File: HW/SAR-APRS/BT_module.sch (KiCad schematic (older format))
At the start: 6 parts

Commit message: schematic update
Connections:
- no-connect marks 0 -> 1
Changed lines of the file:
@@
 Text GLabel 4650 2975 0    50   Input ~ 0
 BT_LED2
+NoConn ~ 5575 3825
 $EndSCHEMATC

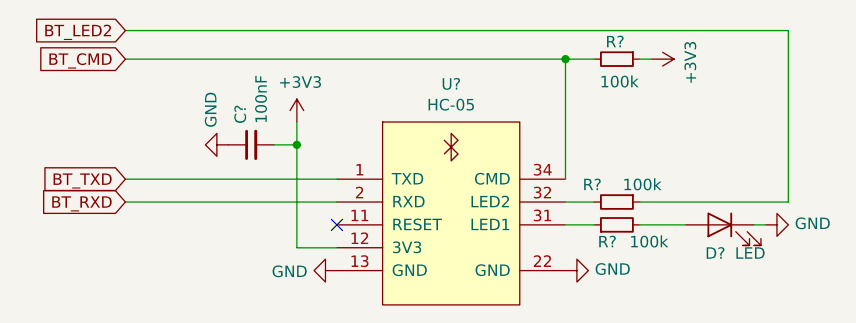
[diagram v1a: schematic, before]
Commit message: schematic update
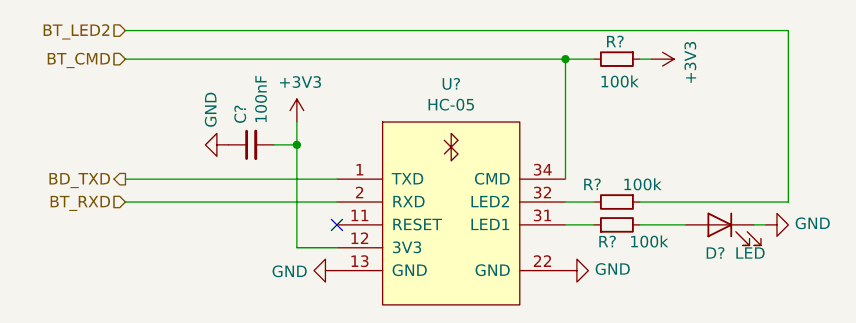
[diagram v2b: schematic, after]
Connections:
- net BT_TXD renamed BD_TXD
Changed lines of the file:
@@
 $Descr A4 11693 8268
 encoding utf-8
-Sheet 6 6
+Sheet 5 6
 Title ""
 Date ""
@@
 Wire Wire Line
 	4650 2975 7550 2975
-Text GLabel 4650 3100 0    50   Input ~ 0
-BT_CMD
 Wire Wire Line
 	4650 3100 6575 3100
-Text GLabel 4650 3625 0    50   Input ~ 0
-BT_TXD
-Text GLabel 4650 3725 0    50   Input ~ 0
-BT_RXD
 Wire Wire Line
 	4650 3625 5575 3625
 Wire Wire Line
 	4650 3725 5575 3725
-Text GLabel 4650 2975 0    50   Input ~ 0
+NoConn ~ 5575 3825
+Text HLabel 4650 2975 0    50   Input ~ 0
 BT_LED2
-NoConn ~ 5575 3825
+Text HLabel 4650 3100 0    50   Input ~ 0
+BT_CMD
+Text HLabel 4650 3625 0    50   Output ~ 0
+BD_TXD
+Text HLabel 4650 3725 0    50   Input ~ 0
+BT_RXD
 $EndSCHEMATC

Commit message: schem and pcb update
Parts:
- gave numbers to parts that had none: 6
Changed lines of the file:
@@
 EESchema Schematic File Version 4
 LIBS:SAR-APRS-cache
-EELAYER 28 0
+EELAYER 29 0
 EELAYER END
 $Descr A4 11693 8268
@@
 $EndDescr
 $Comp
-L power:GND #PWR?
+L power:GND #PWR0142
 U 1 1 5C823DC3
 P 5575 4025
-F 0 "#PWR?" H 5575 3775 50  0001 C CNN
+F 0 "#PWR0142" H 5575 3775 50  0001 C CNN
 F 1 "GND" V 5580 3897 50  0000 R CNN
 F 2 "" H 5575 4025 50  0001 C CNN
@@
 $EndComp
 $Comp
-L power:+3V3 #PWR?
+L power:+3V3 #PWR0143
 U 1 1 5C823DC9
 P 5400 3375
-F 0 "#PWR?" H 5400 3225 50  0001 C CNN
+F 0 "#PWR0143" H 5400 3225 50  0001 C CNN
 F 1 "+3V3" H 5415 3548 50  0000 C CNN
 F 2 "" H 5400 3375 50  0001 C CNN
@@
 	5400 3925 5400 3475
 $Comp
-L device:C_Small C?
+L device:C_Small C22
 U 1 1 5C823DD1
 P 5200 3475
-F 0 "C?" H 5292 3521 50  0000 L CNN
+F 0 "C22" H 5292 3521 50  0000 L CNN
 F 1 "100nF" H 5292 3430 50  0000 L CNN
 F 2 "" H 5200 3475 50  0001 C CNN
@@
 $EndComp
 $Comp
-L power:GND #PWR?
+L power:GND #PWR0144
 U 1 1 5C823DD7
 P 5100 3475
-F 0 "#PWR?" H 5100 3225 50  0001 C CNN
+F 0 "#PWR0144" H 5100 3225 50  0001 C CNN
 F 1 "GND" H 5025 3400 50  0000 R CNN
 F 2 "" H 5100 3475 50  0001 C CNN
@@
 	5300 3475 5400 3475
 $Comp
-L power:GND #PWR?
+L power:GND #PWR0145
 U 1 1 5C823DE0
 P 6575 4025
-F 0 "#PWR?" H 6575 3775 50  0001 C CNN
+F 0 "#PWR0145" H 6575 3775 50  0001 C CNN
 F 1 "GND" V 6580 3897 50  0000 R CNN
 F 2 "" H 6575 4025 50  0001 C CNN
@@
 $EndComp
 $Comp
-L device:R_Small R?
+L device:R_Small R24
 U 1 1 5C823DE6
 P 6800 3725
-F 0 "R?" V 6725 3575 50  0000 L CNN
+F 0 "R24" V 6725 3575 50  0000 L CNN
 F 1 "100k" V 6725 3750 50  0000 L CNN
 F 2 "" H 6800 3725 50  0001 C CNN
@@
 $EndComp
 $Comp
-L device:R_Small R?
+L device:R_Small R25
 U 1 1 5C823DEC
 P 6800 3825
-F 0 "R?" V 6725 3825 50  0000 L CNN
+F 0 "R25" V 6725 3825 50  0000 L CNN
 F 1 "100k" V 6725 3600 50  0000 L CNN
 F 2 "" H 6800 3825 50  0001 C CNN
@@
 	6700 3825 6575 3825
 $Comp
-L device:LED D?
+L device:LED D6
 U 1 1 5C823DF4
 P 7250 3825
-F 0 "D?" H 7225 3700 50  0000 L CNN
+F 0 "D6" H 7225 3700 50  0000 L CNN
 F 1 "LED" H 7050 3700 50  0000 L CNN
 F 2 "" H 7250 3825 50  0001 C CNN
@@
 	7450 3825 7400 3825
 $Comp
-L power:GND #PWR?
+L power:GND #PWR0146
 U 1 1 5C823DFC
 P 7450 3825
-F 0 "#PWR?" H 7450 3575 50  0001 C CNN
+F 0 "#PWR0146" H 7450 3575 50  0001 C CNN
 F 1 "GND" V 7455 3697 50  0000 R CNN
 F 2 "" H 7450 3825 50  0001 C CNN
@@
 $EndComp
 $Comp
-L power:+3V3 #PWR?
+L power:+3V3 #PWR0147
 U 1 1 5C823E02
 P 6950 3100
-F 0 "#PWR?" H 6950 2950 50  0001 C CNN
+F 0 "#PWR0147" H 6950 2950 50  0001 C CNN
 F 1 "+3V3" H 6965 3273 50  0000 C CNN
 F 2 "" H 6950 3100 50  0001 C CNN
@@
 $EndComp
 $Comp
-L APRS_modules:HC-05 U?
+L APRS_modules:HC-05 U8
 U 1 1 5C823E09
 P 6075 3825
-F 0 "U?" H 6075 4440 50  0000 C CNN
+F 0 "U8" H 6075 4440 50  0000 C CNN
 F 1 "HC-05" H 6075 4349 50  0000 C CNN
 F 2 "maxrez:HC-05 BT" H 5575 4175 50  0001 C CNN
@@
 	6950 3100 6900 3100
 $Comp
-L device:R_Small R?
+L device:R_Small R23
 U 1 1 5C823E15
 P 6800 3100
-F 0 "R?" V 6725 3050 50  0000 L CNN
+F 0 "R23" V 6725 3050 50  0000 L CNN
 F 1 "100k" V 6900 3025 50  0000 L CNN
 F 2 "" H 6800 3100 50  0001 C CNN

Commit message: schm and pcb update
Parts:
- C22: footprint (none) -> Capacitors_SMD:C_0603
- R23, R24, R25: footprint (none) -> Resistors_SMD:R_0603
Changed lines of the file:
@@
 F 0 "C22" H 5292 3521 50  0000 L CNN
 F 1 "100nF" H 5292 3430 50  0000 L CNN
-F 2 "" H 5200 3475 50  0001 C CNN
+F 2 "Capacitors_SMD:C_0603" H 5200 3475 50  0001 C CNN
 F 3 "~" H 5200 3475 50  0001 C CNN
 	1    5200 3475
@@
 F 0 "R24" V 6725 3575 50  0000 L CNN
 F 1 "100k" V 6725 3750 50  0000 L CNN
-F 2 "" H 6800 3725 50  0001 C CNN
+F 2 "Resistors_SMD:R_0603" H 6800 3725 50  0001 C CNN
 F 3 "~" H 6800 3725 50  0001 C CNN
 	1    6800 3725
@@
 F 0 "R25" V 6725 3825 50  0000 L CNN
 F 1 "100k" V 6725 3600 50  0000 L CNN
-F 2 "" H 6800 3825 50  0001 C CNN
+F 2 "Resistors_SMD:R_0603" H 6800 3825 50  0001 C CNN
 F 3 "~" H 6800 3825 50  0001 C CNN
 	1    6800 3825
@@
 F 0 "R23" V 6725 3050 50  0000 L CNN
 F 1 "100k" V 6900 3025 50  0000 L CNN
-F 2 "" H 6800 3100 50  0001 C CNN
+F 2 "Resistors_SMD:R_0603" H 6800 3100 50  0001 C CNN
 F 3 "~" H 6800 3100 50  0001 C CNN
 	1    6800 3100

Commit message: PCB update
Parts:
- C22: footprint Capacitors_SMD:C_0603 -> Capacitors_SMD:C_0805
- D6: footprint (none) -> LEDs:LED_0805
- R23, R24, R25: footprint Resistors_SMD:R_0603 -> Resistors_SMD:R_0805
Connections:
- net BD_TXD renamed BT_TXD
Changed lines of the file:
@@
 F 0 "C22" H 5292 3521 50  0000 L CNN
 F 1 "100nF" H 5292 3430 50  0000 L CNN
-F 2 "Capacitors_SMD:C_0603" H 5200 3475 50  0001 C CNN
+F 2 "Capacitors_SMD:C_0805" H 5200 3475 50  0001 C CNN
 F 3 "~" H 5200 3475 50  0001 C CNN
 	1    5200 3475
@@
 F 0 "R24" V 6725 3575 50  0000 L CNN
 F 1 "100k" V 6725 3750 50  0000 L CNN
-F 2 "Resistors_SMD:R_0603" H 6800 3725 50  0001 C CNN
+F 2 "Resistors_SMD:R_0805" H 6800 3725 50  0001 C CNN
 F 3 "~" H 6800 3725 50  0001 C CNN
 	1    6800 3725
@@
 F 0 "R25" V 6725 3825 50  0000 L CNN
 F 1 "100k" V 6725 3600 50  0000 L CNN
-F 2 "Resistors_SMD:R_0603" H 6800 3825 50  0001 C CNN
+F 2 "Resistors_SMD:R_0805" H 6800 3825 50  0001 C CNN
 F 3 "~" H 6800 3825 50  0001 C CNN
 	1    6800 3825
@@
 F 0 "D6" H 7225 3700 50  0000 L CNN
 F 1 "LED" H 7050 3700 50  0000 L CNN
-F 2 "" H 7250 3825 50  0001 C CNN
+F 2 "LEDs:LED_0805" H 7250 3825 50  0001 C CNN
 F 3 "~" H 7250 3825 50  0001 C CNN
 	1    7250 3825
@@
 F 0 "R23" V 6725 3050 50  0000 L CNN
 F 1 "100k" V 6900 3025 50  0000 L CNN
-F 2 "Resistors_SMD:R_0603" H 6800 3100 50  0001 C CNN
+F 2 "Resistors_SMD:R_0805" H 6800 3100 50  0001 C CNN
 F 3 "~" H 6800 3100 50  0001 C CNN
 	1    6800 3100
@@
 BT_CMD
 Text HLabel 4650 3625 0    50   Output ~ 0
-BD_TXD
+BT_TXD
 Text HLabel 4650 3725 0    50   Input ~ 0
 BT_RXD
